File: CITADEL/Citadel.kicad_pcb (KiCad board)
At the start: 2 copper layers, 139.7 x 86.4 mm, 40 parts, among them J1 Conn_01x02_Socket, J2 Conn_01x02_Socket, J3 USB3_A, J4 Conn_01x04_Socket, J5 Conn_01x03_Socket, J6 Conn_01x03_Socket, J7 Conn_01x03_Socket, J8 Conn_01x02_Pin, M1 Motor_DC, M2 Motor_DC, M3 Motor_DC, M4 Motor_DC, M5 Fan_Tacho, M6 Fan_Tacho, M7 Fan_Tacho, Q1 SSM3K329R_LF, Q2 SSM3K329R_LF, Q3 SSM3K329R_LF, Q4 SSM3K329R_LF, Q5 SSM3K329R_LF, Q6 SSM3K329R_LF, Q7 SSM3K329R_LF, U1 DEV-16771

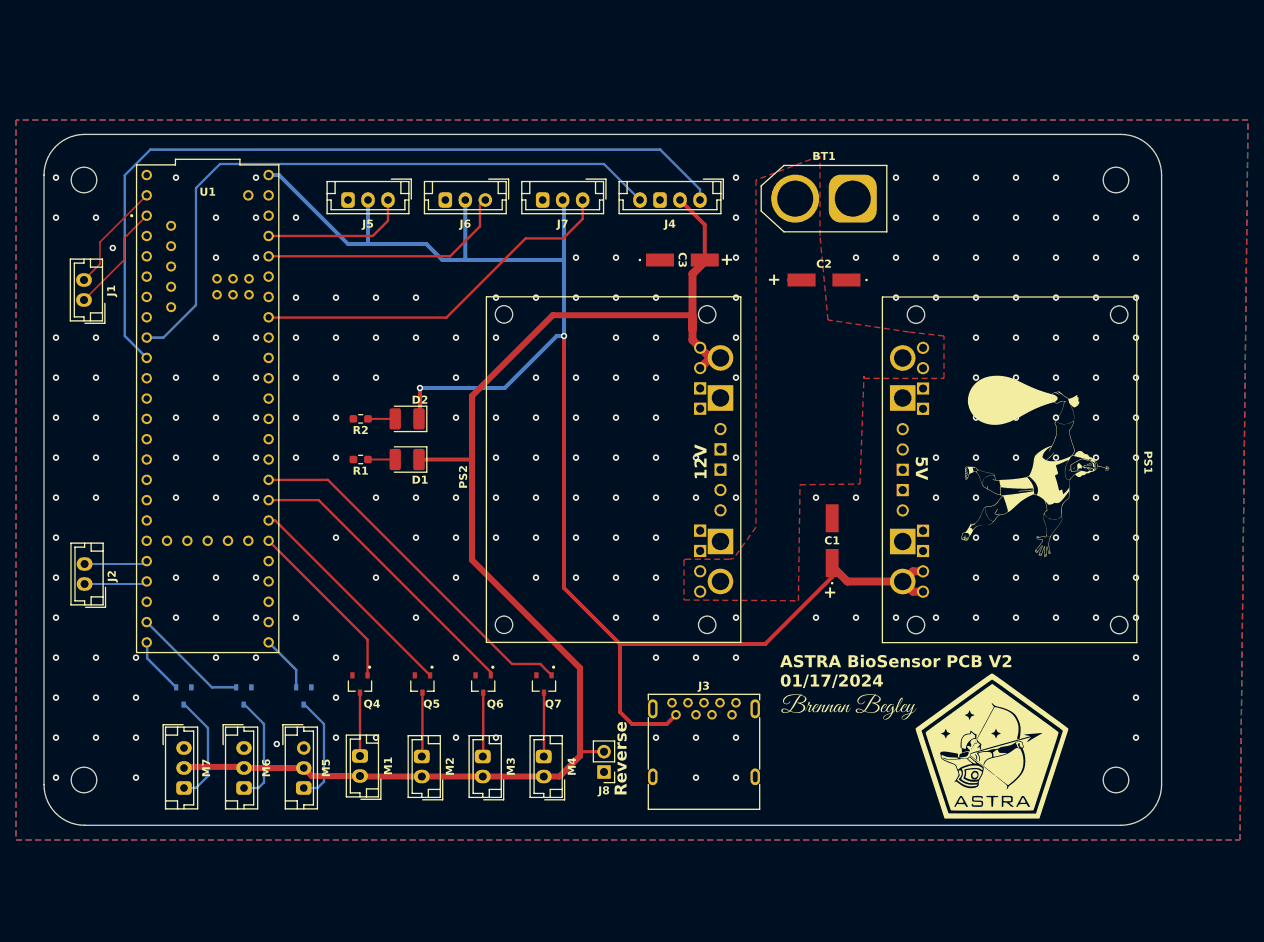
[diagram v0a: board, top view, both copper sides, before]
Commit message: CITADEL 2025 V1, FAERIE 2025 V1
CITADEL January 27, 2025; FAERIE January 26, 2025; Katherine and Mason did CITADEL, Reymund did FAERIE
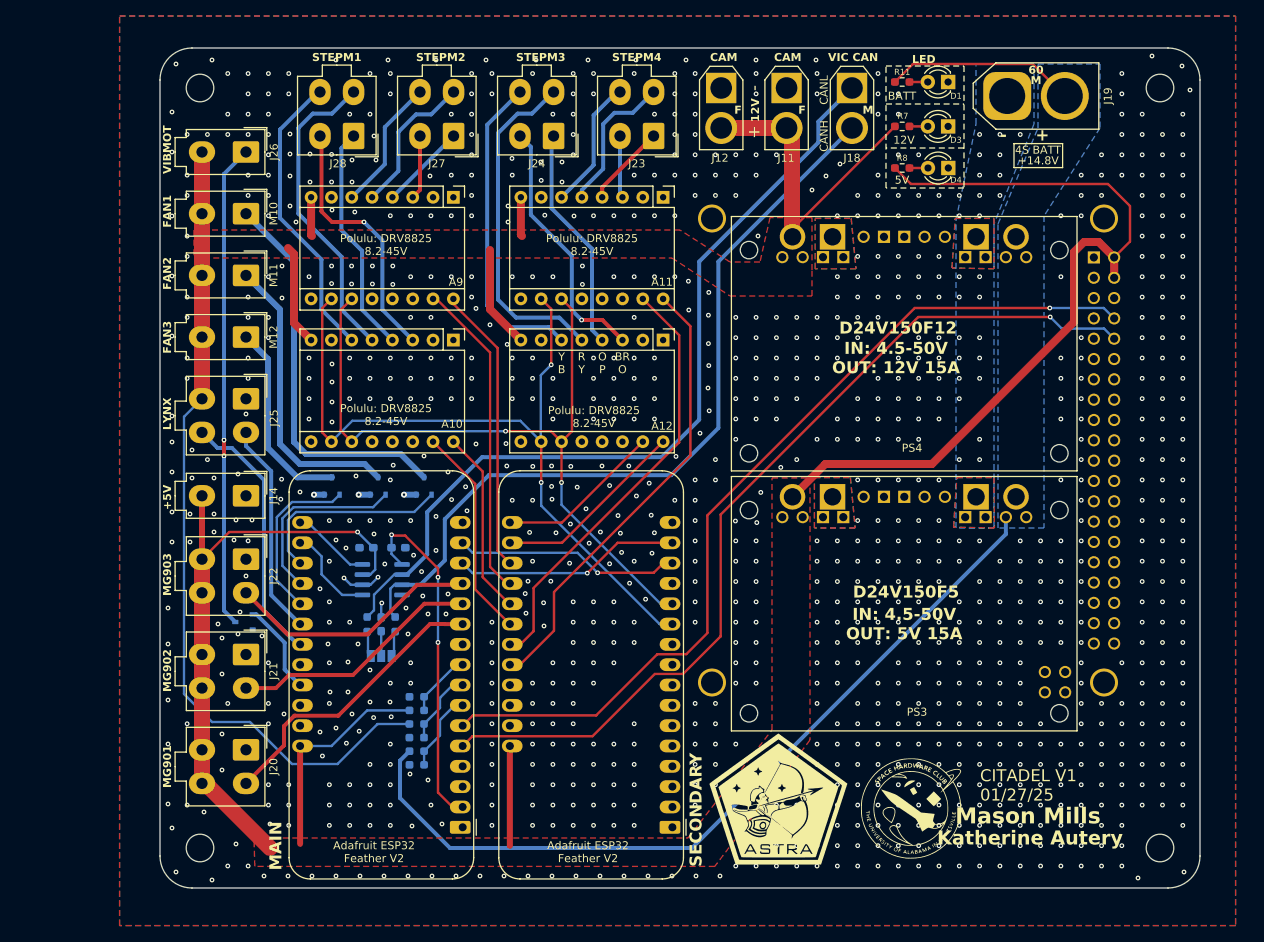
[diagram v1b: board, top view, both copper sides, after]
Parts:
- removed BT1: Battery, Connector_AMASS:AMASS_XT60-F_1x02_P7.20mm_Vertical
- removed D2: LED, LED_SMD:LED_1210_3225Metric_Pad1.42x2.65mm_HandSolder
- removed the G*** at (187.7, 91.8)
- removed the G*** at (182.0, 127.0)
- removed the G*** at (164.0, 122.5)
- removed H1, H2, H3, H4: MountingHole, MountingHole:MountingHole_3.2mm_M3
- removed J1, J2: Conn_01x02_Socket, Connector_JST:JST_EH_B2B-EH-A_1x02_P2.50mm_Vertical
- removed J3: USB3_A, Connector_USB:USB3_A_Molex_48393-001
- removed J4: Conn_01x04_Socket, Connector_JST:JST_EH_B4B-EH-A_1x04_P2.50mm_Vertical
- removed J5, J6, J7: Conn_01x03_Socket, Connector_JST:JST_EH_B3B-EH-A_1x03_P2.50mm_Vertical
- removed J8: Conn_01x02_Pin, Connector_PinHeader_2.54mm:PinHeader_1x02_P2.54mm_Vertical
- removed M1, M2, M3, M4: Motor_DC, Connector_JST:JST_EH_B2B-EH-A_1x02_P2.50mm_Vertical
- removed M5, M6, M7: Fan_Tacho, Connector_JST:JST_EH_B3B-EH-A_1x03_P2.50mm_Vertical
- removed PS1, PS2: ~, D24V150F5:D24V150F5
- removed Q1, Q2, Q3: SSM3K329R_LF, Nmos:SOTFL95P240X88-3N
- removed U1: DEV-16771, Teensy:MODULE_DEV-16771
- added A10: Pololu_Breakout_DRV8825, Module:Pololu_Breakout-16_15.2x20.3mm, F.Cu at (114.7, 76.5)
- added A11: Pololu_Breakout_DRV8825, Module:Pololu_Breakout-16_15.2x20.3mm, F.Cu at (140.9, 58.7)
- added A12: Pololu_Breakout_DRV8825, Module:Pololu_Breakout-16_15.2x20.3mm, F.Cu at (140.9, 76.5)
- added A7: Adafruit Feather ESP32 V2, Module:Adafruit_Feather, F.Cu at (115.8, 137.4)
- added A8: Adafruit Feather ESP32 V2, Module:Adafruit_Feather, F.Cu at (142.1, 137.4)
- added A9: Pololu_Breakout_DRV8825, Module:Pololu_Breakout-16_15.2x20.3mm, F.Cu at (114.7, 58.7)
- added D3: LED, LED_THT:LED_D3.0mm, F.Cu at (176.5, 49.8)
- added D4: LED, LED_THT:LED_D3.0mm, F.Cu at (176.5, 55.0)
- added G***: LOGO, Citadel:ASTRA, F.Cu at (155.3, 133.7)
- added G***: LOGO, LOGO, F.Cu at (172.1, 135.1)
- added J11: Camera 1, Connector_AMASS:AMASS_XT30U-F_1x02_P5.0mm_Vertical, F.Cu at (156.3, 45.0)
- added J12: Camera 2, Connector_AMASS:AMASS_XT30U-F_1x02_P5.0mm_Vertical, F.Cu at (148.2, 45.0)
- added J14: 5V Swtich Power, Connector_Molex:Molex_Mini-Fit_Jr_5566-02A_2x01_P4.20mm_Vertical, F.Cu at (88.8, 96.0)
- added J18: CAN BUS, Connector_AMASS:AMASS_XT30U-F_1x02_P5.0mm_Vertical, F.Cu at (164.5, 45.0)
- added J19: Battery Connections, Connector_AMASS:AMASS_XT60-M_1x02_P7.20mm_Vertical, F.Cu at (183.9, 46.0)
- added J20: Servo 1, Connector_Molex:Molex_Mini-Fit_Jr_5566-04A_2x02_P4.20mm_Vertical, F.Cu at (88.8, 127.7)
- added J21: Servo 2, Connector_Molex:Molex_Mini-Fit_Jr_5566-04A_2x02_P4.20mm_Vertical, F.Cu at (88.8, 115.8)
- added J22: Servo 3, Connector_Molex:Molex_Mini-Fit_Jr_5566-04A_2x02_P4.20mm_Vertical, F.Cu at (88.8, 103.9)
- added J23: Stepper Motors 3, Connector_Molex:Molex_Mini-Fit_Jr_5566-04A_2x02_P4.20mm_Vertical, F.Cu at (139.7, 51.0)
- added J24: Stepper Motors 4, Connector_Molex:Molex_Mini-Fit_Jr_5566-04A_2x02_P4.20mm_Vertical, F.Cu at (127.2, 51.0)
- added J25: LSS Servo, Connector_Molex:Molex_Mini-Fit_Jr_5566-04A_2x02_P4.20mm_Vertical, F.Cu at (88.8, 83.8)
- added J26: Vibration Motor, Connector_Molex:Molex_Mini-Fit_Jr_5566-02A_2x01_P4.20mm_Vertical, F.Cu at (88.8, 53.0)
- added J27: Stepper Motors 1, Connector_Molex:Molex_Mini-Fit_Jr_5566-04A_2x02_P4.20mm_Vertical, F.Cu at (114.7, 51.0)
- added J28: Stepper Motors 2, Connector_Molex:Molex_Mini-Fit_Jr_5566-04A_2x02_P4.20mm_Vertical, F.Cu at (102.2, 51.0)
- added JP1: SolderJumper_3_Open, Jumper:SolderJumper-3_P1.3mm_Open_Pad1.0x1.5mm, B.Cu at (105.7, 116.0)
- added M10: Fan 1, Connector_Molex:Molex_Mini-Fit_Jr_5566-02A_2x01_P4.20mm_Vertical, F.Cu at (88.8, 60.7)
- added M11: Fan 2, Connector_Molex:Molex_Mini-Fit_Jr_5566-02A_2x01_P4.20mm_Vertical, F.Cu at (88.8, 68.4)
- added M12: Fan 3, Connector_Molex:Molex_Mini-Fit_Jr_5566-02A_2x01_P4.20mm_Vertical, F.Cu at (88.8, 76.1)
- added PS3: ~, Citadel:D24V15OF5, F.Cu at (172.6, 129.5)
- added PS4: ~, Citadel:D24V15OF5, F.Cu at (172.6, 97.0)
- added R10: 10 kΩ, Resistor_SMD:R_0603_1608Metric_Pad0.98x0.95mm_HandSolder, B.Cu at (110.1, 121.1)
- added R11: 1000, Resistor_SMD:R_0603_1608Metric_Pad0.98x0.95mm_HandSolder, F.Cu at (170.8, 44.2)
- added R3: R_US, Resistor_SMD:R_0603_1608Metric_Pad0.98x0.95mm_HandSolder, B.Cu at (107.4, 112.0)
- added R4: 10 kΩ, Resistor_SMD:R_0603_1608Metric_Pad0.98x0.95mm_HandSolder, B.Cu at (110.1, 124.5)
- added R5: 3.8 kΩ, Resistor_SMD:R_0603_1608Metric_Pad0.98x0.95mm_HandSolder, B.Cu at (110.1, 126.2)
- added R6: R_US, Resistor_SMD:R_0603_1608Metric_Pad0.98x0.95mm_HandSolder, B.Cu at (103.9, 112.0)
- added R7: 1000, Resistor_SMD:R_0603_1608Metric_Pad0.98x0.95mm_HandSolder, F.Cu at (170.8, 49.8)
- added R8: 1000, Resistor_SMD:R_0603_1608Metric_Pad0.98x0.95mm_HandSolder, F.Cu at (170.8, 55.0)
- added R9: 10 kΩ, Resistor_SMD:R_0603_1608Metric_Pad0.98x0.95mm_HandSolder, B.Cu at (110.1, 122.8)
- added REF**: 4-40 Mounting Hole, Citadel:4-40 Mounting Hole, F.Cu at (203.0, 45.0)
- added REF**: 4-40 Mounting Hole, Citadel:4-40 Mounting Hole, F.Cu at (83.0, 45.0)
- added REF**: 4-40 Mounting Hole, Citadel:4-40 Mounting Hole, F.Cu at (203.0, 140.0)
- added REF**: 4-40 Mounting Hole, Citadel:4-40 Mounting Hole, F.Cu at (83.0, 140.0)
- added U3: TJA1051T-3, Package_SO:SOIC-8_3.9x4.9mm_P1.27mm, B.Cu at (105.8, 106.5)
- added U4: RASPBERRY_PI_4B_4GB, Module:MODULE_RASPBERRY_PI_4B_4GB, F.Cu at (171.5, 100.3)
- C1, C2, C3: value 875105345011 -> C; footprint Caps:CAP_WCAP-PSLP_6P3X7P7_WRE -> Capacitor_SMD:C_0603_1608Metric_Pad1.08x0.95mm_HandSolder; moved to B.Cu
- D1: footprint LED_SMD:LED_1210_3225Metric_Pad1.42x2.65mm_HandSolder -> LED_THT:LED_D3.0mm
- Q4, Q5, Q6: footprint Nmos:SOTFL95P240X88-3N -> Citadel:SSM3K329_LF; moved to B.Cu
- Q7: value SSM3K329R_LF -> ~; footprint Nmos:SOTFL95P240X88-3N -> Citadel:SSM3K329_LF; moved to B.Cu
- R1: value 1000 -> 10 kΩ; moved to B.Cu
- R2: value 1000 -> 3.1 kΩ; moved to B.Cu
- moved D1 82.5 mm to (176.5, 44.2)
- moved C2 66.3 mm to (103.8, 102.5), turned to 0 degrees
- moved C3 59.1 mm to (105.7, 112.0), turned to -90 degrees
- moved C1 54.2 mm to (107.8, 102.5), turned to 0 degrees
- moved R2 43.8 mm to (110.1, 129.6)
- moved Q7 38.3 mm to (88.5, 111.8), turned to 180 degrees
- moved R1 37.1 mm to (110.1, 127.9), turned to 0 degrees
- moved Q6 25.8 mm to (111.0, 94.8), turned to 90 degrees
- moved Q5 25.4 mm to (105.2, 94.8), turned to 90 degrees
- moved Q4 25.0 mm to (99.5, 94.8), turned to 90 degrees
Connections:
- C1 pad 1: +5V -> +3.3V
- C2 pad 2: +BATT -> +5V
- C3 pad 2: +12V -> Net-(JP1-C)
- D1 pad 1: +12V -> GND
- Q4 pad 1: /M1MOS Signal -> /Fan3MosSignal
- Q4 pad 3: /M1MOS -> /Fan3MOS
- Q5 pad 1: /M2MOS Signal -> /Fan2MosSignal
- Q5 pad 3: /M2MOS -> /Fan2MOS
- Q6 pad 1: /M3MOS Signal -> /Fan1MosSignal
- Q6 pad 3: /M3MOS -> /Fan1MOS
- Q7 pad 1: /M4MOS Signal -> /VibMotorSignal
- Q7 pad 3: /M4MOS -> /VibMotorMOS
- R1 pad 1: Net-(D1-A) -> +BATT
- R1 pad 2: GND -> /BATT_ADC
- R2 pad 1: Net-(D2-A) -> /BATT_ADC
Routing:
- net +BATT: track 1.02 -> 126.9 mm
- net /RPRX: track 0.00 -> 113.7 mm, vias 0 -> 1
- net /RPTX: track 0.00 -> 112.2 mm, vias 0 -> 1
- net /CIT_CAN-: track 0.00 -> 105.3 mm
- net /CIT_CAN+: track 0.00 -> 100.5 mm
- net /M0: track 0.00 -> 96.6 mm, vias 0 -> 2
- net /M1: track 0.00 -> 92.1 mm, vias 0 -> 2
- net /Lynx RX: track 100.6 -> 26.8 mm
- net /VibMotorMOS: track 0.00 -> 60.5 mm, vias 0 -> 2
- net /DIR_Motor3: track 0.00 -> 57.2 mm
- net /STEP_Motor3: track 0.00 -> 54.6 mm
- net /Lynx TX: track 81.1 -> 32.8 mm
- net /Cap1PWM: track 46.7 -> 0.00 mm
- net /M4MOS Signal: track 45.5 -> 0.00 mm
- net +3.3V: track 0.00 -> 43.6 mm, vias 0 -> 3
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- added copper zone on F.Cu, net +12V
- added copper zone on F.Cu, net +5V
- added copper zone on B.Cu, net +BATT
- removed copper zone on F.Cu, net +BATT
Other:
- board size 139.7 x 86.4 mm -> 130 x 105 mm
- board text added: "+14.8V"
- board text added: "+5V"
- board text added: "- +"
- board text added: "0.1 μF"
- board text added: "1.0 μF"
- board text added: "10 kΩ"
- board text added: "3.1 kΩ"
- board text added: "3.8 kΩ"
- board text added: "4.7 nF"
- board text added: "4S BATT"
- board text added: "60"
- board text added: "60Ω"
- board text added: "Adafruit ESP32 Feather V2"
- board text added: "B"
- board text added: "BATT"
- board text added: "BR"
- board text added: "CAM"
- board text added: "CAN Transceiver"
- board text added: "CITADEL V1 01/27/25"
- board text added: "D24V150F12"
- board text added: "D24V150F5"
- board text added: "F"
- board text added: "FAN1"
- board text added: "FAN2"
- board text added: "FAN3"
- board text added: "IN: 4.5-50V OUT: 12V 15A"
- board text added: "IN: 4.5-50V OUT: 5V 15A"
- board text added: "Katherine Autery"
- board text added: "LED"
- board text added: "LYNX"
- board text added: "M"
- board text added: "MAIN"
- board text added: "MG901"
- board text added: "MG902"
- board text added: "MG903"
- board text added: "Mason Mills"
- board text added: "O"
- board text added: "P"
- board text added: "Polulu: DRV8825 8.2-45V"
- board text added: "R"
- board text added: "RASPBERRY_PI_4B IN: 5V 1A"
- board text added: "SECONDARY"
- board text added: "SSM3K329R_LF"
- board text added: "STEPM1"
- board text added: "STEPM2"
- board text added: "STEPM3"
- board text added: "STEPM4"
- board text added: "TJA1051T/3"
- board text added: "VIBMOT"
- board text added: "VIC CAN"
- board text added: "Y"
- board text removed: "+"
- board text removed: "ASTRA BioSensor PCB V2 01/17/2024"
- board text removed: "Reverse"

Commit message: CITADEL 2025 V2
April 8, 2025; replaced the second MCU with a GPIO extender IC that didn't end up working
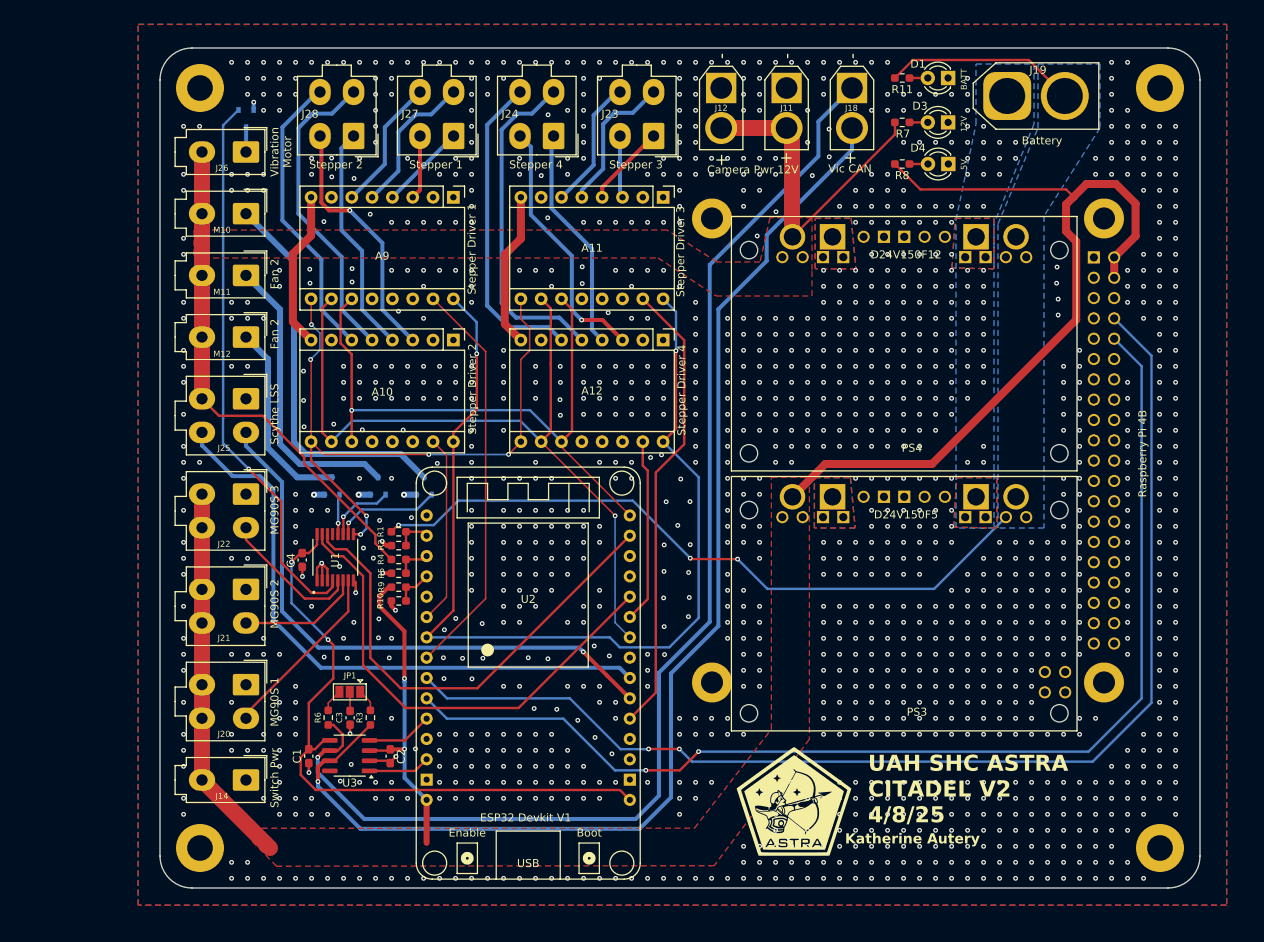
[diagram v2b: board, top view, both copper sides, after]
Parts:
- removed A7, A8: Adafruit Feather ESP32 V2, Module:Adafruit_Feather
- removed the G*** at (155.3, 133.7)
- removed the REF** at (203.0, 45.0)
- removed the REF** at (83.0, 45.0)
- removed the REF** at (203.0, 140.0)
- removed the REF** at (83.0, 140.0)
- added C4: 0.047uF, Capacitor_SMD:C_0603_1608Metric_Pad1.08x0.95mm_HandSolder, F.Cu at (95.8, 104.0)
- added REF**: 3mm Hole, Core_fp:3mm Hole, F.Cu at (83.0, 140.0)
- added REF**: 3mm Hole, Core_fp:3mm Hole, F.Cu at (203.0, 140.0)
- added REF**: 3mm Hole, Core_fp:3mm Hole, F.Cu at (203.0, 45.0)
- added REF**: 3mm Hole, Core_fp:3mm Hole, F.Cu at (83.0, 45.0)
- added U1: MAX7315AUE_T, Citadel:MAX7315AUE+T, F.Cu at (99.9, 103.7)
- added U2: ~, Citadel:esp32_devkit_v1, F.Cu at (124.0, 98.4)
- C1, C2, C3, JP1, R1, R10, R2, R3, R4, R5, R6, R9, U3: moved to F.Cu
- Q7: value ~ -> SSM3K329R_LF
- moved Q7 62.9 mm to (88.8, 48.8), turned to -90 degrees
- moved J14 35.5 mm to (88.8, 131.5)
- moved C1 28.4 mm to (96.6, 128.5), turned to -90 degrees
- moved R1 27.5 mm to (107.8, 100.5)
- moved R2 27.5 mm to (107.8, 102.2)
- moved C2 26.2 mm to (106.8, 128.5), turned to 90 degrees
- moved U3 22.4 mm to (101.7, 128.5), turned to 180 degrees
- moved R4 20.7 mm to (107.8, 103.9)
- moved R5 20.7 mm to (107.8, 105.7)
- moved R9 15.6 mm to (107.8, 107.4)
- moved G*** 14.9 mm to (157.2, 134.0)
- moved R6 12.6 mm to (99.0, 123.7), turned to -90 degrees
- moved C3 12.3 mm to (101.8, 123.7), turned to 90 degrees
- moved R10 12.2 mm to (107.8, 109.1)
- moved R3 12.1 mm to (104.3, 123.7), turned to -90 degrees
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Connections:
- A10 pad 16: /DIR_Motor2 -> /DIR
- A10 pad 9: unconnected-(A10-~{EN}-Pad9) -> /Step_Motor_Enable
- A11 pad 16: /DIR_Motor3 -> /DIR
- A11 pad 9: unconnected-(A11-~{EN}-Pad9) -> /Step_Motor_Enable
- A12 pad 16: /DIR_Motor4 -> /DIR
- A12 pad 9: unconnected-(A12-~{EN}-Pad9) -> /Step_Motor_Enable
- A9 pad 16: /DIR_Motor1 -> /DIR
- A9 pad 9: unconnected-(A9-~{EN}-Pad9) -> /Step_Motor_Enable
- U4 pad 10: /RPRX -> /RASPI_TX
- U4 pad 8: /RPTX -> /RASPI_RX
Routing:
- net /RASPI_RX: track 0.00 -> 148.0 mm, vias 0 -> 2
- net /RASPI_TX: track 0.00 -> 143.2 mm, vias 0 -> 2
- net /DIR: track 0.00 -> 125.8 mm, vias 0 -> 2
- net /RPRX: track 113.7 -> 0.00 mm, vias 1 -> 0
- net /RPTX: track 112.2 -> 0.00 mm, vias 1 -> 0
- net /Step_Motor_Enable: track 0.00 -> 81.1 mm, vias 0 -> 6
- net /MAX_SDA: track 0.00 -> 60.4 mm
- net /MAX_SCL: track 0.00 -> 60.4 mm
- net /VibMotorSignal: track 11.3 -> 69.5 mm, vias 0 -> 1
- net /VibMotorMOS: track 60.5 -> 3.09 mm, vias 2 -> 0
- net /DIR_Motor3: track 57.2 -> 0.00 mm
- net /CIT_CAN+: track 100.5 -> 152.1 mm, vias 0 -> 1
- net /CIT_CAN-: track 105.3 -> 154.1 mm, vias 0 -> 1
- net /Lynx RX: track 26.8 -> 72.2 mm, vias 0 -> 1
- net /Lynx TX: track 32.8 -> 76.7 mm
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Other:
- board text added: "Battery"
- board text added: "Camera Pwr 12V"
- board text added: "ESP32 Devkit V1"
- board text added: "Fan 2"
- board text added: "MG90S 1"
- board text added: "MG90S 2"
- board text added: "MG90S 3"
- board text added: "Raspberry Pi 4B"
- board text added: "Scythe LSS"
- board text added: "Stepper 1"
- board text added: "Stepper 2"
- board text added: "Stepper 3"
- board text added: "Stepper 4"
- board text added: "Stepper Driver 1"
- board text added: "Stepper Driver 2"
- board text added: "Stepper Driver 3"
- board text added: "Stepper Driver 4"
- board text added: "Switch Pwr"
- board text added: "UAH SHC ASTRA CITADEL V2 4/8/25"
- board text added: "Vibration Motor"
- board text added: "Vic CAN"
- board text removed: "+14.8V"
- board text removed: "+5V"
- board text removed: "- +"
- board text removed: "0.1 μF"
- board text removed: "1.0 μF"
- board text removed: "10 kΩ"
- board text removed: "3.1 kΩ"
- board text removed: "3.8 kΩ"
- board text removed: "4.7 nF"
- board text removed: "4S BATT"
- board text removed: "60"
- board text removed: "60Ω"
- board text removed: "Adafruit ESP32 Feather V2"
- board text removed: "B"
- board text removed: "BR"
- board text removed: "CAM"
- board text removed: "CAN Transceiver"
- board text removed: "CITADEL V1 01/27/25"
- board text removed: "F"
- board text removed: "FAN1"
- board text removed: "FAN2"
- board text removed: "FAN3"
- board text removed: "IN: 4.5-50V OUT: 12V 15A"
- board text removed: "IN: 4.5-50V OUT: 5V 15A"
- board text removed: "LED"
- board text removed: "LYNX"
- board text removed: "M"
- board text removed: "MAIN"
- board text removed: "MG901"
- board text removed: "MG902"
- board text removed: "MG903"
- board text removed: "Mason Mills"
- board text removed: "O"
- board text removed: "P"
- board text removed: "Polulu: DRV8825 8.2-45V"
- board text removed: "R"
- board text removed: "RASPBERRY_PI_4B IN: 5V 1A"
- board text removed: "SECONDARY"
- board text removed: "SSM3K329R_LF"
- board text removed: "STEPM1"
- board text removed: "STEPM2"
- board text removed: "STEPM3"
- board text removed: "STEPM4"
- board text removed: "TJA1051T/3"
- board text removed: "VIBMOT"
- board text removed: "VIC CAN"
- board text removed: "Y"
